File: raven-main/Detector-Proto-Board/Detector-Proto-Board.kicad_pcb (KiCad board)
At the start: 2 copper layers, 31.8 x 32 mm, 25 parts, among them IC1 ADA4817-1ARDZ-R7, J1 Conn_01x04, U9 TLV3201AIDCKT

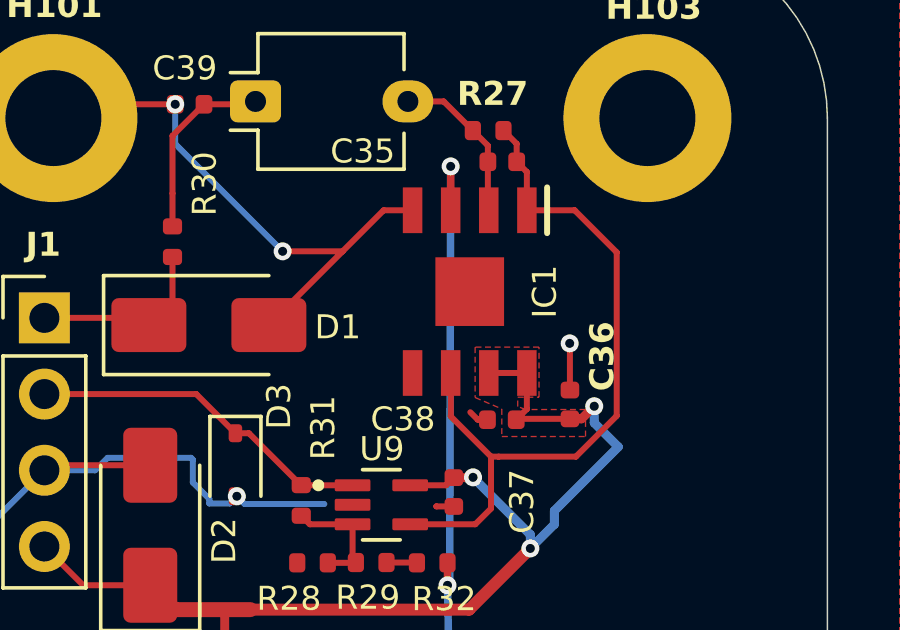
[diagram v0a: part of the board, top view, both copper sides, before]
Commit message: Fixed missing connections on power
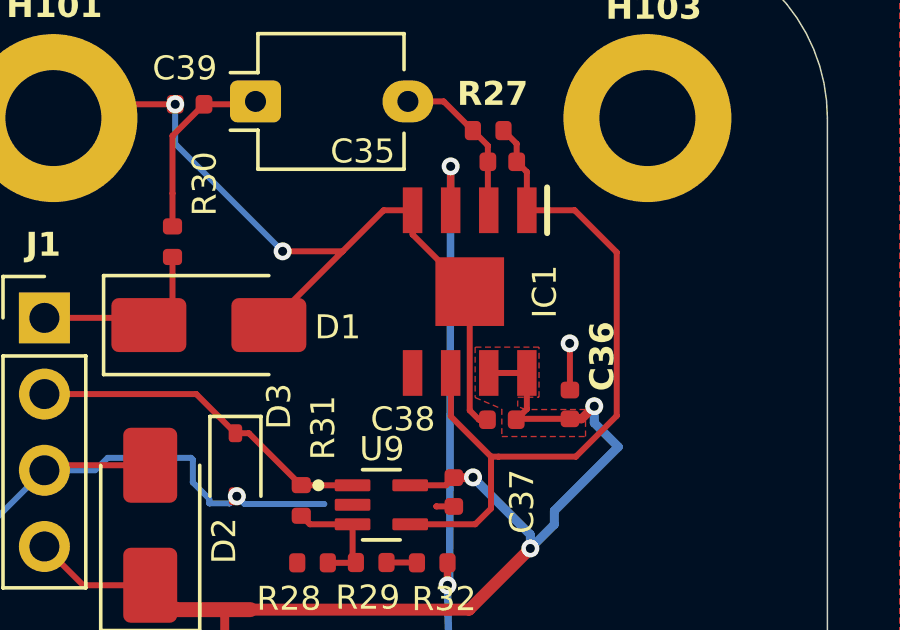
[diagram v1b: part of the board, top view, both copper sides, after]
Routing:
- net GND: track 47.1 -> 54.6 mm
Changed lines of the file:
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@@
+	)
+	(segment
+		(start 116.757499 82.045)
+		(end 116.4775 82.045)
+		(width 0.2)
+		(layer "F.Cu")
+		(net "GND")
 	)
 	(segment
@@
 	)
 	(segment
-		(start 116.437499 82.045)
-		(end 116.187499 81.795)
+		(start 116.167499 77.775)
+		(end 114.262499 75.87)
 		(width 0.2)
 		(layer "F.Cu")
@@
 	)
 	(segment
-		(start 111.93125 76.43125)
-		(end 113.299501 75.063)
+		(start 116.4775 82.045)
+		(end 116.167499 81.734999)
 		(width 0.2)
 		(layer "F.Cu")
@@
 	)
 	(segment
-		(start 116.757499 82.045)
-		(end 116.437499 82.045)
+		(start 116.167499 81.734999)
+		(end 116.167499 77.775)
+		(width 0.2)
+		(layer "F.Cu")
+		(net "GND")
+	)
+	(segment
+		(start 111.93125 76.43125)
+		(end 113.299501 75.063)
 		(width 0.2)
 		(layer "F.Cu")
@@
 		(width 0.2)
 		(layer "F.Cu")
+		(net "GND")
+	)
+	(segment
+		(start 114.262499 75.87)
+		(end 114.262499 75.063)
+		(width 0.2)
+		(layer "F.Cu")

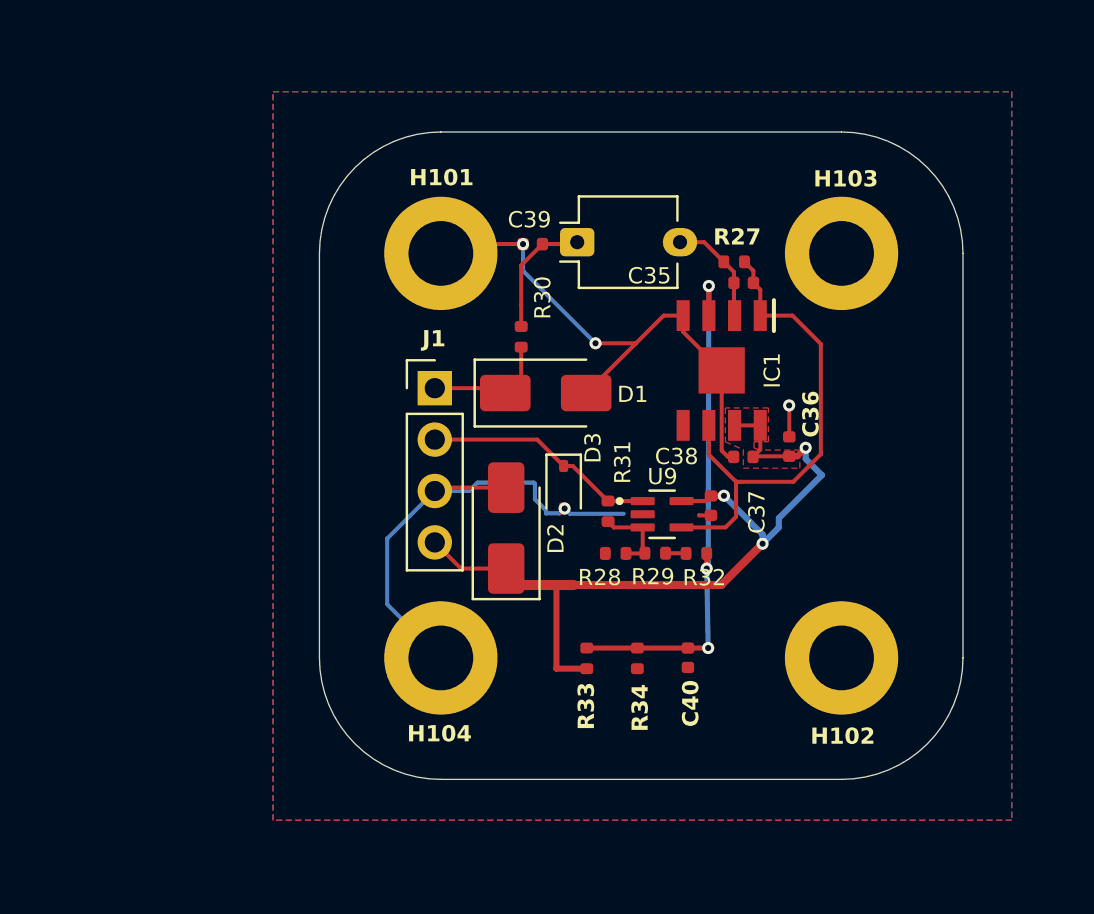
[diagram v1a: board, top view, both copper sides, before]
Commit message: Added some initial pcb changes from Revision 2
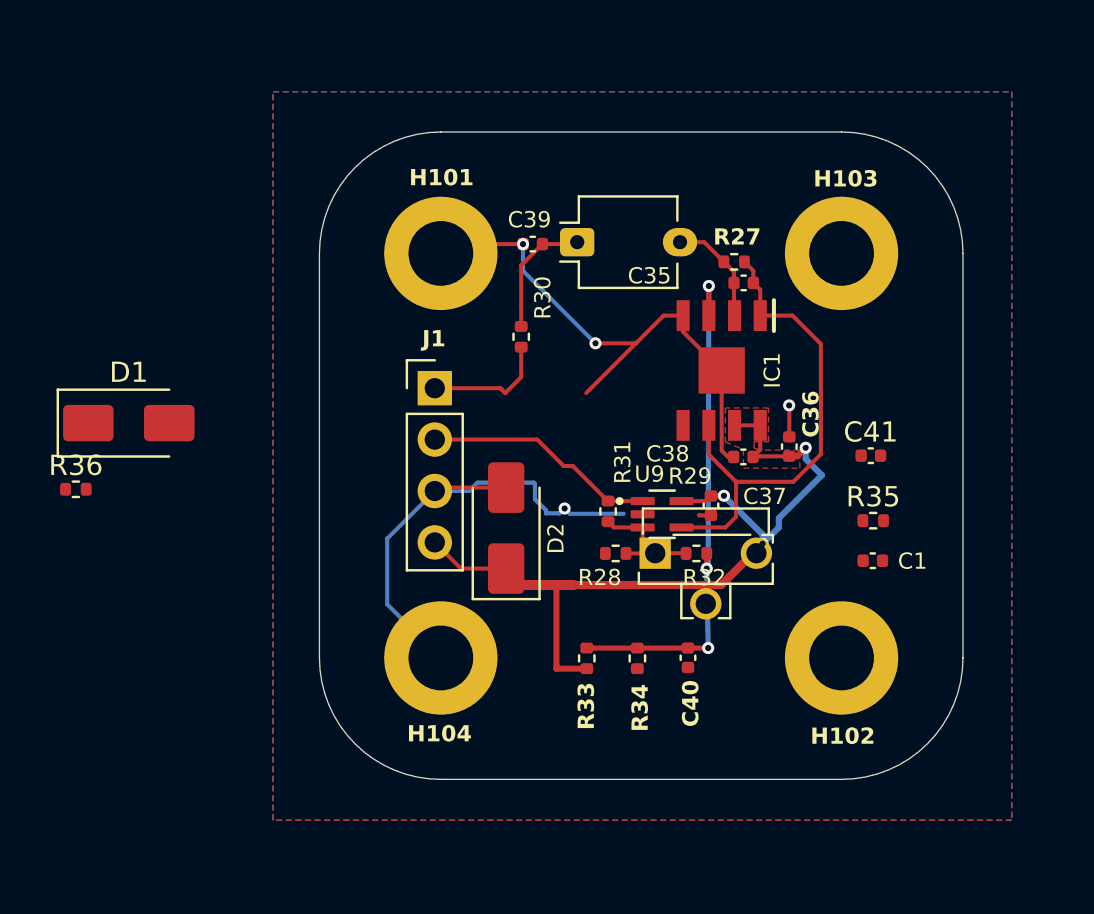
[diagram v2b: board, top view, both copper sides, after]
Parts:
- removed D3: PESD5V0S1BA, Diode_SMD:D_SOD-323
- added C1: 330p, Capacitor_SMD:C_0402_1005Metric, F.Cu at (123.6, 87.2)
- added C41: 0.5pF, Capacitor_SMD:C_0402_1005Metric, F.Cu at (123.5, 82.0)
- added R35: 1.6k, Resistor_SMD:R_0402_1005Metric, F.Cu at (123.7, 85.2)
- added R36: 1G, Resistor_SMD:R_0402_1005Metric, F.Cu at (84.3, 83.6)
- D1: value SMAJ58A -> SMAJ26A
- R29: footprint Resistor_SMD:R_0402_1005Metric -> Potentiometer_THT:Potentiometer_Runtron_RM-063_Horizontal
- R31: value 300K -> 390K
- R32: value 300 -> 33
- moved D1 20.7 mm to (86.9, 80.4)
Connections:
- R28 pad 1: /V_thresh_A -> Net-(R1-Pad1)
- R29 pad 1: /V_thresh_A -> Net-(R1-Pad1)
- U9 pad 4: /OUT -> Net-(U9-IN-)

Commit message: Updated pcb schematic for proto board
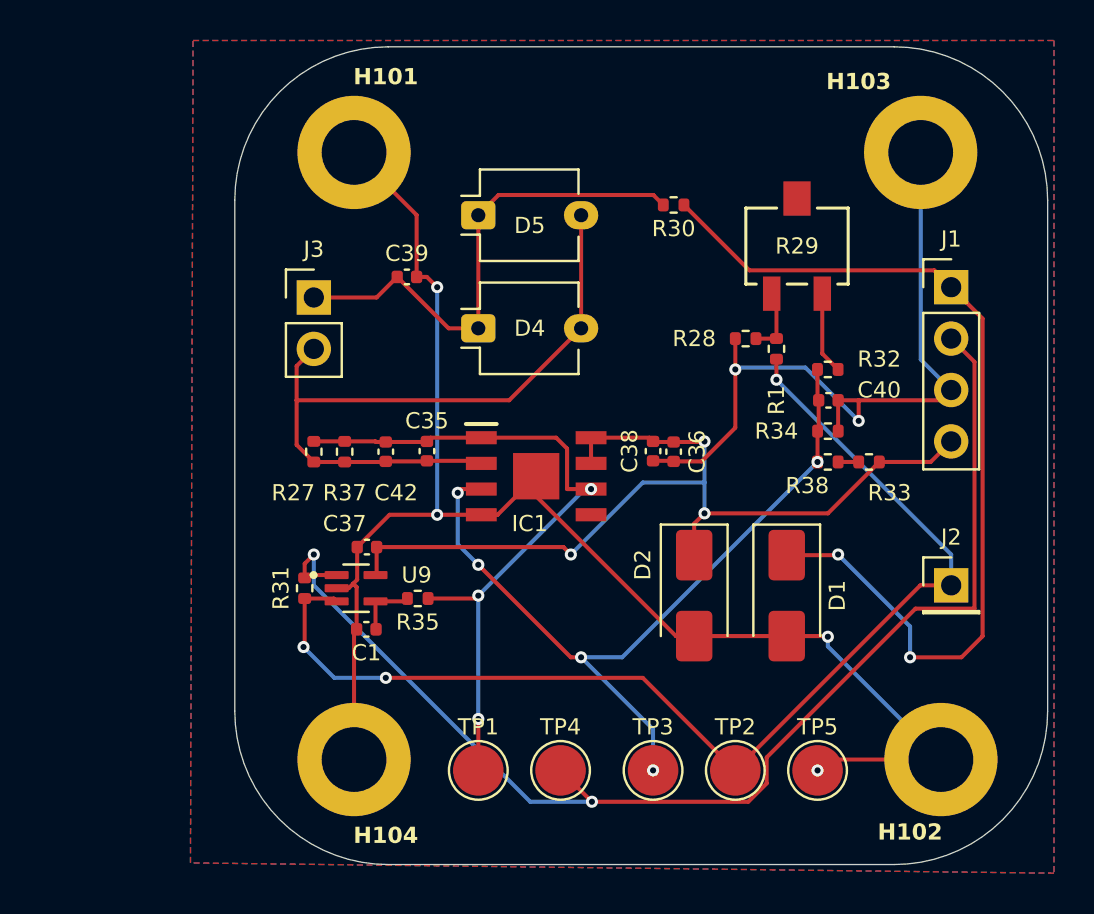
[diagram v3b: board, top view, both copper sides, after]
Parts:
- removed C41: 0.5pF, Capacitor_SMD:C_0402_1005Metric
- removed R36: 1G, Resistor_SMD:R_0402_1005Metric
- added C42: 0.5pF, Capacitor_SMD:C_0402_1005Metric, F.Cu at (99.6, 81.8)
- added D5: BPW34, OptoDevice:Osram_DIL2_4.3x4.65mm_P5.08mm, F.Cu at (104.1, 70.1)
- added J2: Conn_01x01, Connector_PinHeader_2.54mm:PinHeader_1x01_P2.54mm_Vertical, F.Cu at (127.5, 88.4)
- added J3: Conn_01x02, Connector_PinHeader_2.54mm:PinHeader_1x02_P2.54mm_Vertical, F.Cu at (96.0, 74.2)
- added R1: 0, Resistor_SMD:R_0402_1005Metric, F.Cu at (118.9, 76.7)
- added R37: 1G, Resistor_SMD:R_0402_1005Metric, F.Cu at (97.5, 81.8)
- added R38: 0, Resistor_SMD:R_0402_1005Metric, F.Cu at (121.4, 82.3)
- added TP1: OUT, TestPoint:TestPoint_Pad_D2.5mm, F.Cu at (104.1, 97.5)
- added TP2: V_thresh, TestPoint:TestPoint_Pad_D2.5mm, F.Cu at (116.8, 97.5)
- added TP3: Vped, TestPoint:TestPoint_Pad_D2.5mm, F.Cu at (112.8, 97.5)
- added TP4: Detector_Out, TestPoint:TestPoint_Pad_D2.5mm, F.Cu at (108.2, 97.5)
- added TP5: GND, TestPoint:TestPoint_Pad_D2.5mm, F.Cu at (120.9, 97.5)
- R29: footprint Potentiometer_THT:Potentiometer_Runtron_RM-063_Horizontal -> 3224X:SOT_502E
- moved D1 33.6 mm to (119.4, 88.9), turned to -90 degrees
- moved J1 26.0 mm to (127.5, 73.7)
- moved C1 25.3 mm to (98.6, 90.6), turned to 180 degrees
- moved R35 22.8 mm to (101.1, 89.0), turned to 180 degrees
- moved R27 22.8 mm to (96.0, 81.8), turned to 90 degrees
- moved C35 17.7 mm to (101.6, 81.8), turned to 90 degrees
- moved C37 17.1 mm to (98.6, 86.5), turned to 0 degrees
- moved R33 17.0 mm to (123.4, 82.3), turned to 180 degrees
- moved R29 16.7 mm to (119.9, 71.6)
- moved U9 15.6 mm to (98.1, 88.5)
- moved R31 15.5 mm to (95.6, 88.5)
- moved R34 14.7 mm to (121.4, 80.8), turned to 0 degrees
- moved C40 14.5 mm to (121.4, 79.2), turned to 0 degrees
- moved R28 12.4 mm to (117.3, 76.2)
- moved R32 11.2 mm to (121.4, 77.7), turned to 0 degrees
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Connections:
- net +50V renamed +25V
- R33 pad 2: /Vped -> Net-(R33-Pad2)
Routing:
- net GND: track 54.6 -> 111.9 mm, vias 4 -> 6
- net /V_thresh_A: track 4.09 -> 57.1 mm, vias 0 -> 3
- net /Detector_Out_A: track 11.5 -> 62.3 mm, vias 0 -> 2
- net +25V: track 6.55 -> 45.9 mm, vias 0 -> 2
- net Net-(D4-A): track 5.44 -> 35.8 mm
- net Net-(D4-K): track 6.85 -> 24.9 mm
- net /Vped: track 26.2 -> 39.6 mm, vias 3 -> 5
- net /OUT: track 24.7 -> 35.3 mm, vias 0 -> 3
- net +5V: track 41.0 -> 45.7 mm
- net Net-(R1-Pad1): track 0.00 -> 3.33 mm
- net Net-(R29-Pad2): track 1.02 -> 4.07 mm
- net Net-(U9-IN-): track 0.00 -> 3.03 mm
- net Net-(R33-Pad2): track 0.00 -> 1.02 mm
- removed copper zone on F.Cu, net +5V
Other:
- board size 31.8 x 32 mm -> 40.2 x 40.4 mm

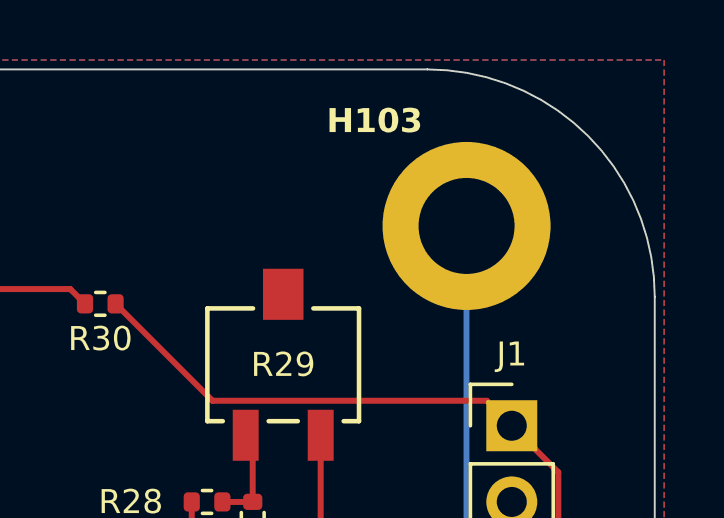
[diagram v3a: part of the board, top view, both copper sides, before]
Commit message: Corrected misaligned drill hole
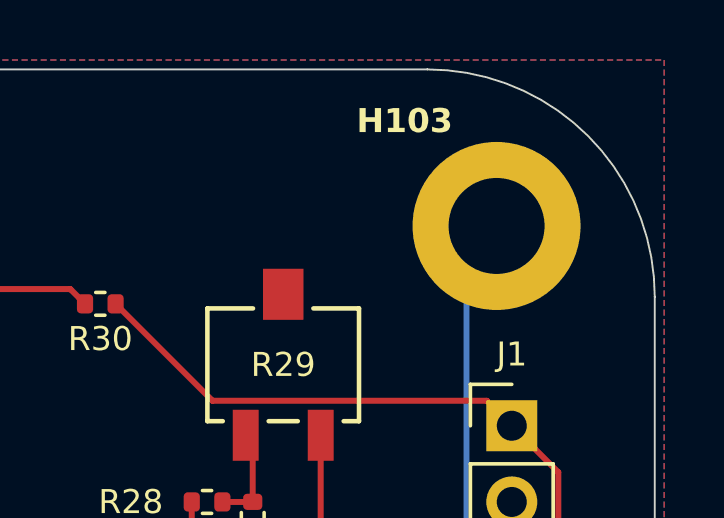
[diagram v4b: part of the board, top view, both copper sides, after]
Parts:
- moved H103 1.00 mm to (127.0, 67.0)
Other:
- board text added: "Designed by Luke Pugsley"
- board text added: "and Peter Dunneice"

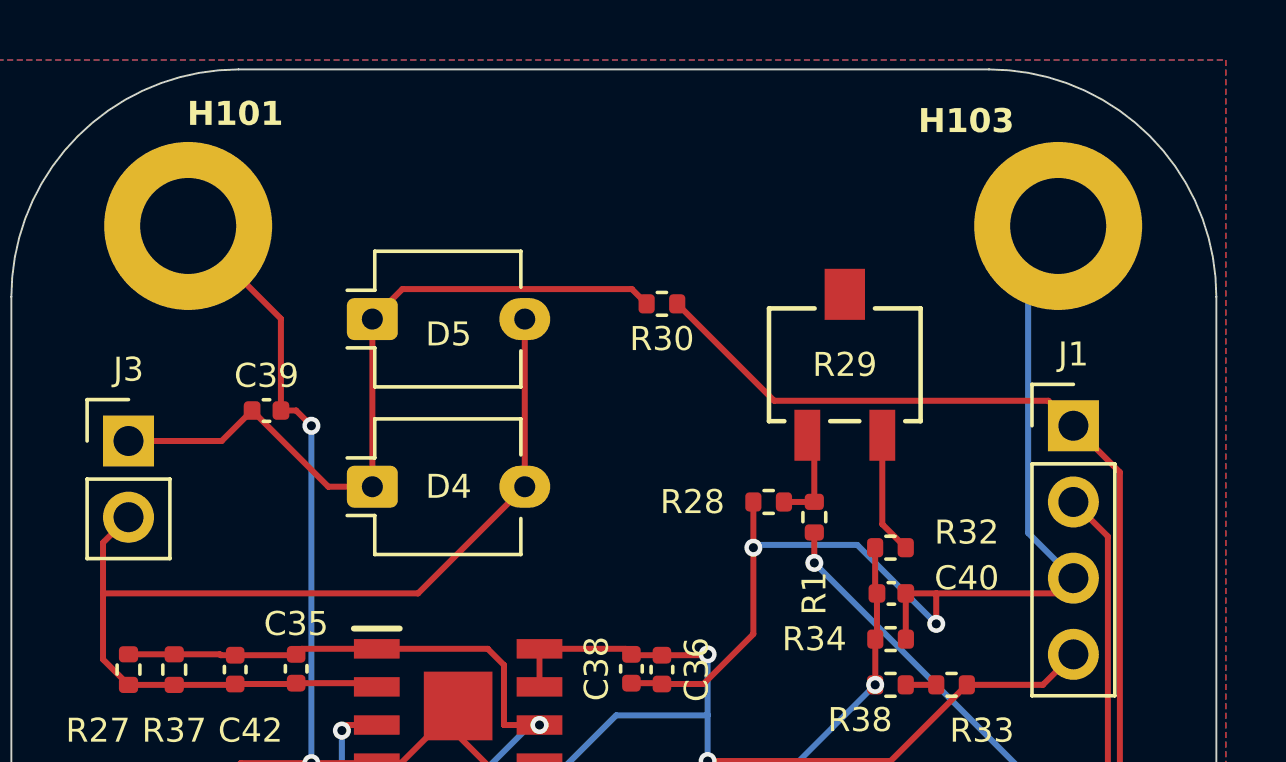
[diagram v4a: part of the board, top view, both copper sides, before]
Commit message: Added draft logos to front and back
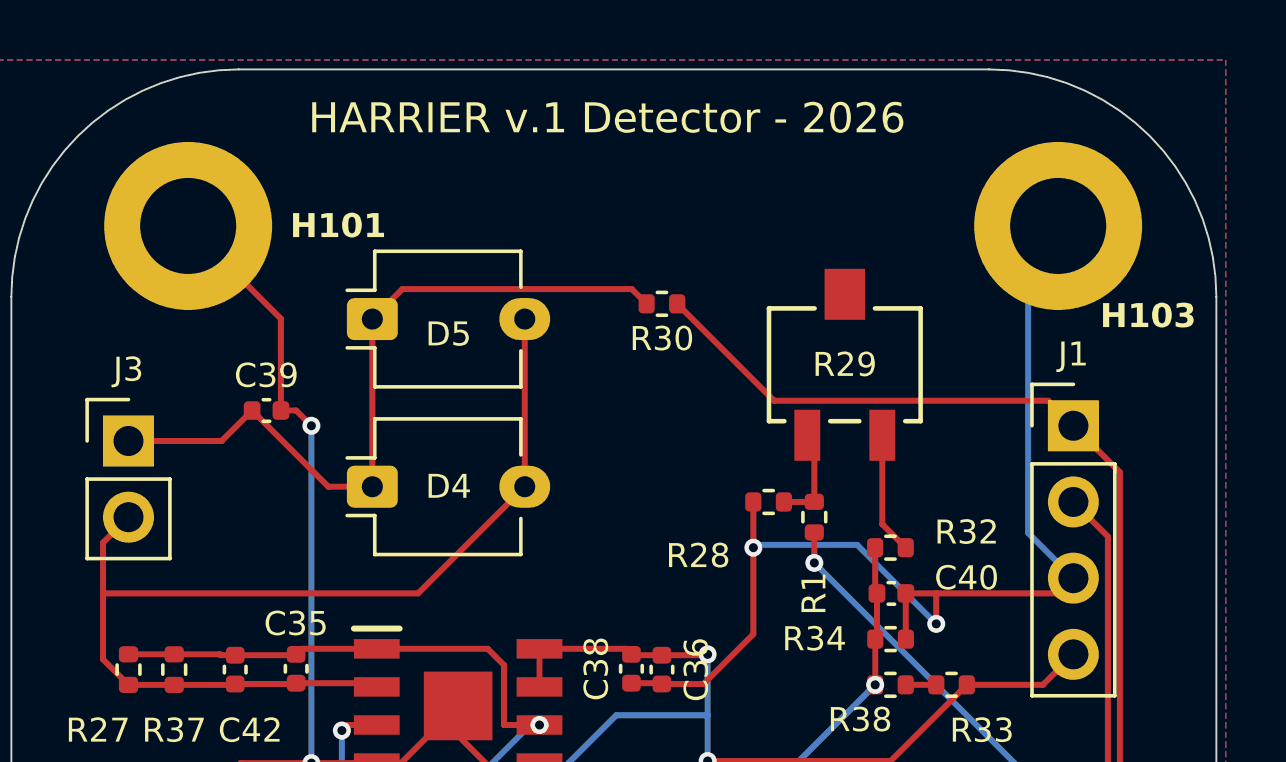
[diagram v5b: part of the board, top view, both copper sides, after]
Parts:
- added G***: LOGO, Decor:iclr_logo_inverted, B.Cu at (104.0, 88.0)
- added G***: LOGO, Decor:harrier-draft, B.Cu at (118.0, 87.0)
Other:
- board text added: "HARRIER v.1 Detector - 2026"

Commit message: Added corrected deco detials
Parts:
- added G***: LOGO, Decor:iclr_logo_small, F.Cu at (121.0, 65.0)
- moved G*** 3.16 mm to (105.0, 85.0)
- moved G*** 3.16 mm to (119.0, 84.0)
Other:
- board text added: "Designed by"
- board text added: "HARRIER v1.0 Detector"
- board text added: "Luke Pugsley and Peter Dunneice"
- board text added: "Payload 2026"
- board text removed: "Designed by Luke Pugsley"
- board text removed: "HARRIER v.1 Detector - 2026"
- board text removed: "and Peter Dunneice"
